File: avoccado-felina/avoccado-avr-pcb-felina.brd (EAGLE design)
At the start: 42 x 17.4 mm, 76 parts, among them Q1 16MHz, Q2 FET, U1 MPU-6000QFN-24, U2 MCP73831

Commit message: no airwires left :+1:  :shaved_ice:
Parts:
- removed JP22: M01NOSILK-KIT, SparkFun-Connectors:1X01NS-KIT
- removed JP26: M01PTH, SparkFun-Connectors:1X01
- added TP12, TP13, TP14: TPTP20R, testpad:TP20R
- TP4: value TEST-POINT3 -> TPTP20R; device SparkFun-Passives:PAD.03X.03 -> testpad:TP20R
- moved JP7 24.4 mm to (63.8, 16.8)
- moved C10 23.8 mm to (35.2, 26.2)
- moved R3 23.7 mm to (62.5, 20.3)
- moved R6 23.7 mm to (60.7, 20.3)
- moved D1 23.7 mm to (64.0, 20.3)
- moved R4 23.7 mm to (58.9, 20.3)
- moved C11 23.6 mm to (55.9, 20.1)
- moved C2 23.6 mm to (57.1, 22.6)
- moved C5 23.6 mm to (57.9, 16.5)
- moved C7 23.6 mm to (28.1, 12.2)
- moved C8 23.6 mm to (55.9, 22.6)
- moved JP10 23.6 mm to (55.9, 25.4)
- moved JP12 23.6 mm to (30.5, 25.4)
- moved JP13 23.6 mm to (30.5, 22.9)
- moved JP14 23.6 mm to (30.5, 20.3)
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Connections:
- net 3.3V: now also TP13.TP
- net 5V: now also TP14.TP; no longer TP4.P$1
- net A3: no longer JP22.1
- net GND: now also TP12.TP, TP4.TP; no longer JP26.1
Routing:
- net GND: track 203.9 -> 227.7 mm, vias 8 -> 9
- net 5V: track 19.0 -> 20.9 mm
- net D7: track 8.94 -> 10.1 mm
- net N$4: track 8.49 -> 9.25 mm
- net N$5: track 4.64 -> 5.40 mm
- net 3.3V: track 162.9 -> 163.7 mm
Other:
- board size 42 x 17.4 mm -> 42.5 x 17.5 mm
- board text added: "5V"
- board text added: "o"
- board text removed: "A2"
- board text removed: "G"
- board text removed: "V"

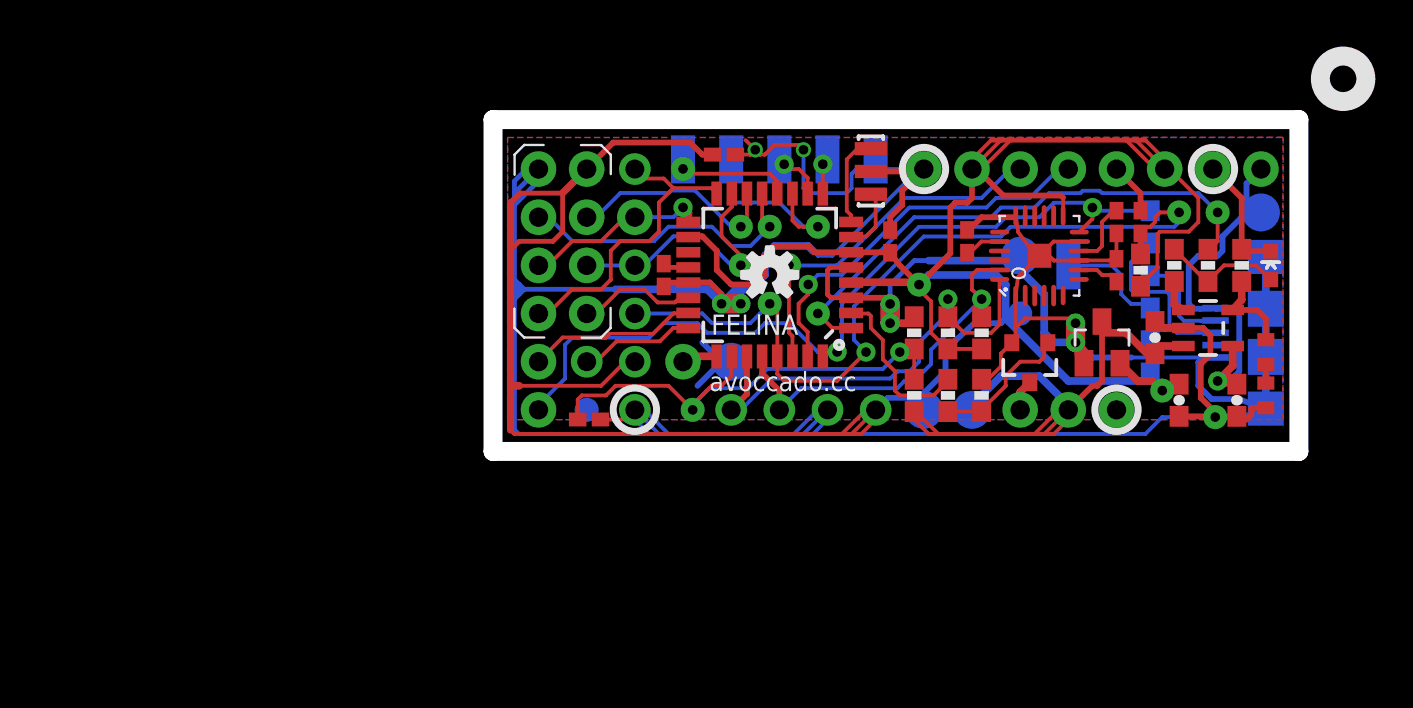
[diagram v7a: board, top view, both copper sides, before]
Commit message: cleanup schematics, add fiducials
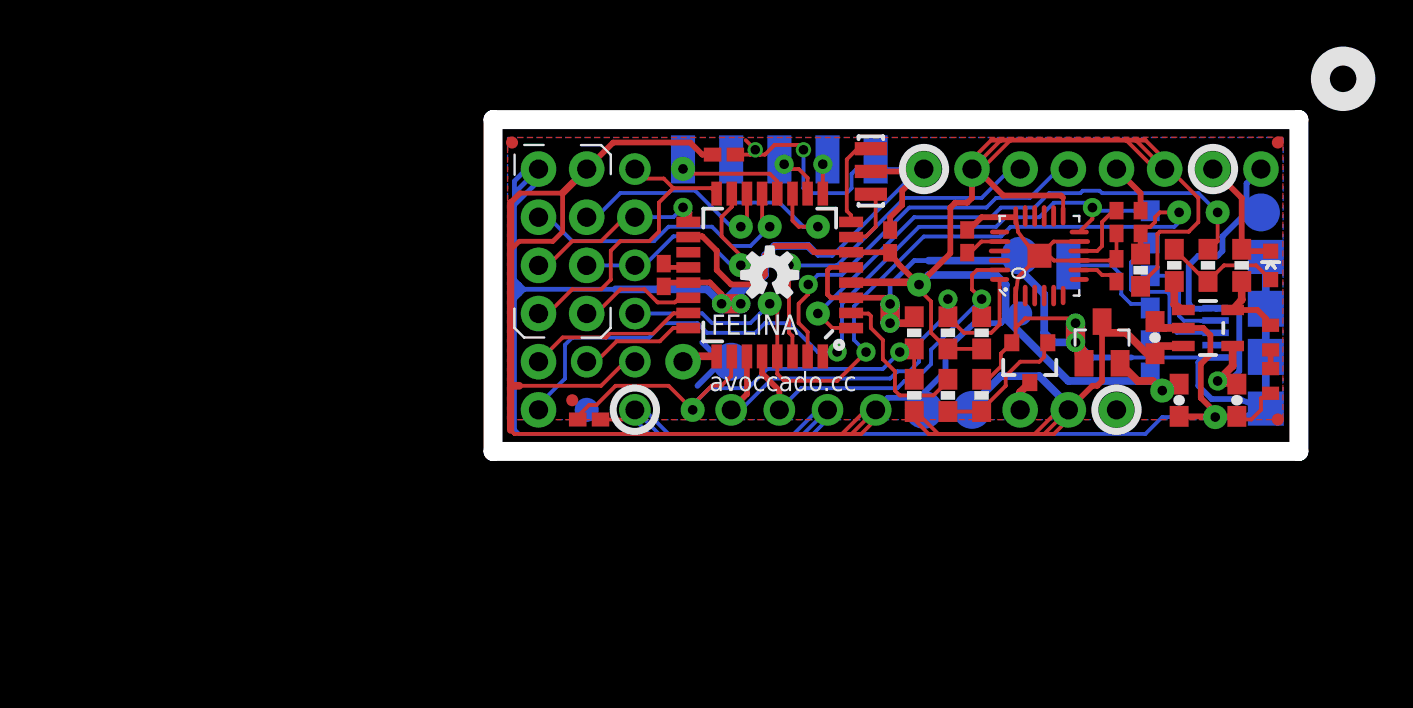
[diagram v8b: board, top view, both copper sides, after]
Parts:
- removed LOGO2: OSHW-LOGOS, SparkFun-Aesthetics:OSHW-LOGO-S
- added FID1, FID2, FID3, FID4: FIDUCIALUFIDUCIAL, SparkFun-Aesthetics:MICRO-FIDUCIAL
- added LOGO1: OSHW-LOGOS, SparkFun-Aesthetics:OSHW-LOGO-S
- moved R12 0.80 mm to (64.0, 16.5)
- moved R9 0.80 mm to (64.0, 14.2)
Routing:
- net GND: track 227.7 -> 228.4 mm
- net CHG-PROG: track 4.74 -> 4.06 mm
- net A3: track 26.7 -> 26.2 mm
